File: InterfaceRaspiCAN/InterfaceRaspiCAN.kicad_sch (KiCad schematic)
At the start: 30 parts, among them J1 Raspberry_Pi_2_3, J10 Conn_02x01, J11 Conn_02x01, J12 Conn_02x01, J13 Conn_01x02, J14 Conn_01x02, J15 Conn_01x02, J16 Conn_01x02, J2 CAN1, J3 CAN2, J4 I2C1_5, J5 I2C2_5, U1 MCP2517FD-xSL, U2 MCP2558FD-xSN, U3 PCF8574A, U4 PESD1CAN, Y2 40MHz

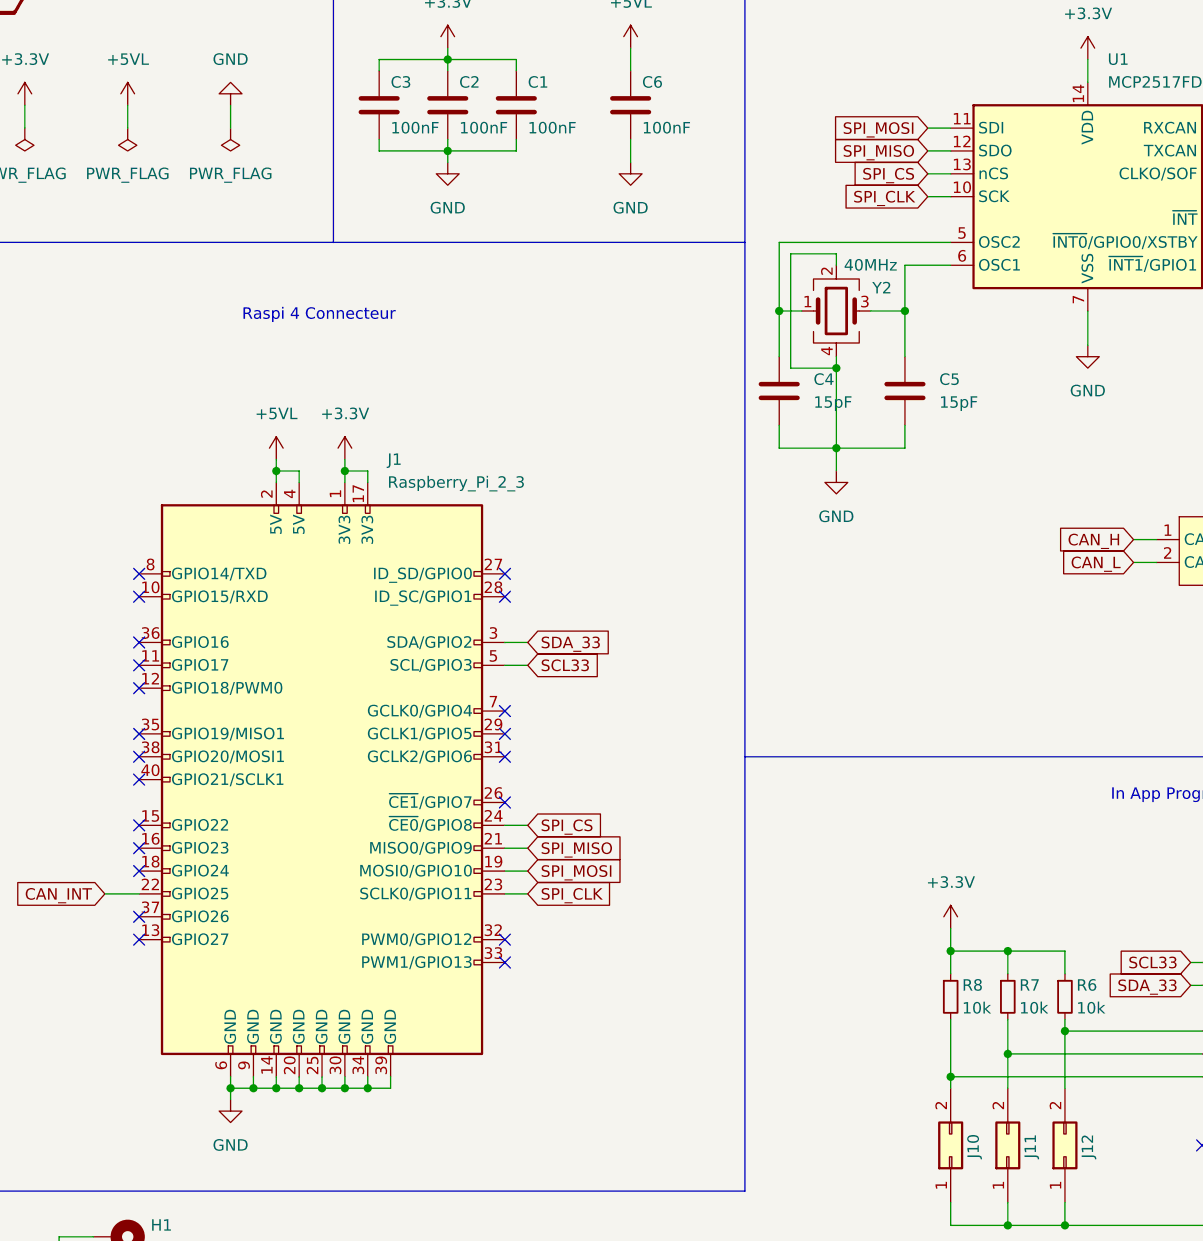
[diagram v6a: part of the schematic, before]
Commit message: Upgrade to KiCad 8 and finish routing
- MasterAlimCAN
- InterfaceRaspiCAN
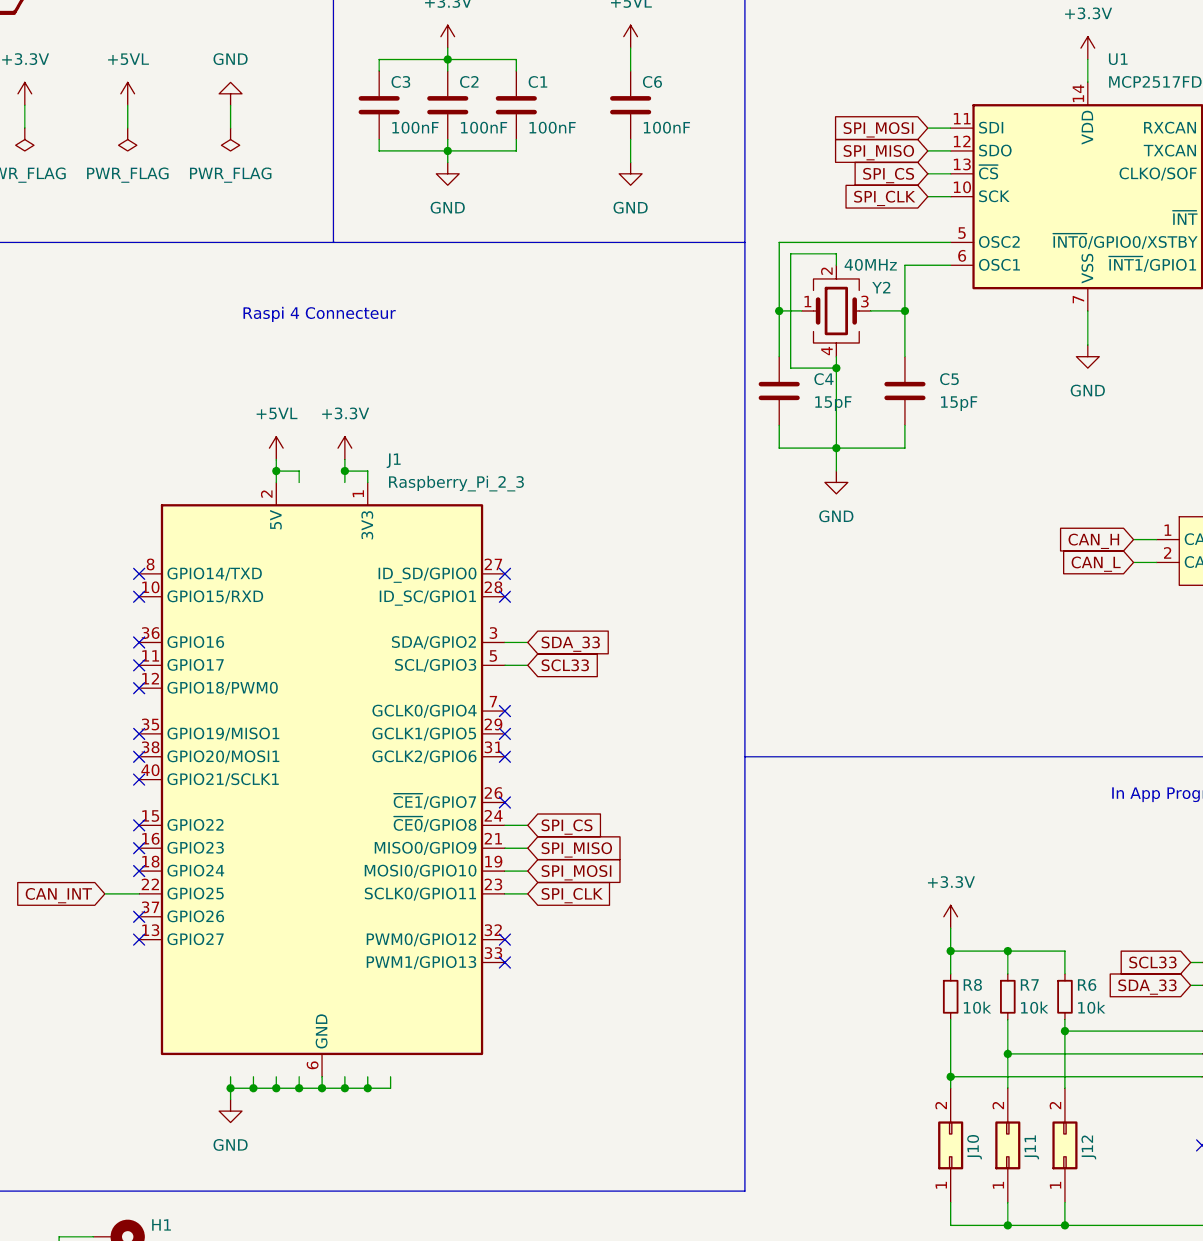
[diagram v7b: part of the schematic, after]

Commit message: Generate all production files
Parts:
- C1, C2, C3, C6: LCSC Part (none) -> C1525
- C4, C5: value 15pF -> 12pF; LCSC Part (none) -> C1547
- R6, R7, R8: LCSC Part (none) -> C17414
- U1: LCSC Part (none) -> C133861
- U2: LCSC Part (none) -> C124015
- U3: LCSC Part (none) -> C7605
- U4: LCSC Part (none) -> C907838
- Y2: BOM JLCPCB Part TZ0475B -> (none); LCSC Part (none) -> C252255
